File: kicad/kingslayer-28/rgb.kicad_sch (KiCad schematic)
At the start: 36 parts, among them IC2 IS31FL3731-QFLS2-TR

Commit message: assign some footprints
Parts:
- D29, D30, D31, D32, D33, D34, D35, D36, D37, D38, D39, D40, D41, D42, D43, D44, D45, D46, D47, D48, D49, D50, D51, D52, D53, D54, D55, D56: footprint (none) -> acheron_Components:LED_RGB_SMD_6028_2.8x3.5mm
- IC2: footprint QFN40P400X400X80-29N -> IS31FL3731-QFLS2-TR:QFN40P400X400X80-29N
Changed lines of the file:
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@@
       (effects (font (size 1.27 1.27)) (justify left))
     )
-    (property "Footprint" "" (at 76.2 78.74 0)
+    (property "Footprint" "acheron_Components:LED_RGB_SMD_6028_2.8x3.5mm" (at 76.2 78.74 0)
       (effects (font (size 1.27 1.27)) hide)
     )
@@
       (effects (font (size 1.27 1.27)) (justify left))
     )
-    (property "Footprint" "" (at 57.15 111.76 0)
+    (property "Footprint" "acheron_Components:LED_RGB_SMD_6028_2.8x3.5mm" (at 57.15 111.76 0)
       (effects (font (size 1.27 1.27)) hide)
     )
@@
       (effects (font (size 1.27 1.27)) (justify left))
     )
-    (property "Footprint" "" (at 95.25 111.76 0)
+    (property "Footprint" "acheron_Components:LED_RGB_SMD_6028_2.8x3.5mm" (at 95.25 111.76 0)
       (effects (font (size 1.27 1.27)) hide)
     )
@@
     )
     (property "Footprint" "" (at 259.08 133.35 0)
-      (effects (font (size 1.524 1.524)))
+      (effects (font (size 1.524 1.524)) hide)
     )
     (property "Datasheet" "" (at 259.08 133.35 0)
@@
       (effects (font (size 1.27 1.27)) (justify left))
     )
-    (property "Footprint" "" (at 57.15 78.74 0)
+    (property "Footprint" "acheron_Components:LED_RGB_SMD_6028_2.8x3.5mm" (at 57.15 78.74 0)
       (effects (font (size 1.27 1.27)) hide)
     )
@@
       (effects (font (size 1.27 1.27)) (justify left))
     )
-    (property "Footprint" "" (at 38.1 144.78 0)
+    (property "Footprint" "acheron_Components:LED_RGB_SMD_6028_2.8x3.5mm" (at 38.1 144.78 0)
       (effects (font (size 1.27 1.27)) hide)
     )
@@
       (effects (font (size 1.27 1.27)) (justify left))
     )
-    (property "Footprint" "" (at 57.15 45.72 0)
+    (property "Footprint" "acheron_Components:LED_RGB_SMD_6028_2.8x3.5mm" (at 57.15 45.72 0)
       (effects (font (size 1.27 1.27)) hide)
     )
@@
       (effects (font (size 1.27 1.27)) (justify left))
     )
-    (property "Footprint" "" (at 38.1 45.72 0)
+    (property "Footprint" "acheron_Components:LED_RGB_SMD_6028_2.8x3.5mm" (at 38.1 45.72 0)
       (effects (font (size 1.27 1.27)) hide)
     )
@@
       (effects (font (size 1.27 1.27)) (justify left))
     )
-    (property "Footprint" "" (at 99.06 177.8 0)
+    (property "Footprint" "acheron_Components:LED_RGB_SMD_6028_2.8x3.5mm" (at 99.06 177.8 0)
       (effects (font (size 1.27 1.27)) hide)
     )
@@
     )
     (property "Footprint" "" (at 190.5 146.05 0)
-      (effects (font (size 1.524 1.524)))
+      (effects (font (size 1.524 1.524)) hide)
     )
     (property "Datasheet" "~" (at 190.5 146.05 0)
@@
       (effects (font (size 1.27 1.27)) (justify left))
     )
-    (property "Footprint" "" (at 133.35 144.78 0)
+    (property "Footprint" "acheron_Components:LED_RGB_SMD_6028_2.8x3.5mm" (at 133.35 144.78 0)
       (effects (font (size 1.27 1.27)) hide)
     )
@@
       (effects (font (size 1.27 1.27)) (justify left))
     )
-    (property "Footprint" "" (at 57.15 177.8 0)
+    (property "Footprint" "acheron_Components:LED_RGB_SMD_6028_2.8x3.5mm" (at 57.15 177.8 0)
       (effects (font (size 1.27 1.27)) hide)
     )
@@
       (effects (font (size 1.27 1.27)) (justify left))
     )
-    (property "Footprint" "" (at 118.11 177.8 0)
+    (property "Footprint" "acheron_Components:LED_RGB_SMD_6028_2.8x3.5mm" (at 118.11 177.8 0)
       (effects (font (size 1.27 1.27)) hide)
     )
@@
     )
     (property "Footprint" "" (at 198.12 50.8 0)
-      (effects (font (size 1.524 1.524)))
+      (effects (font (size 1.524 1.524)) hide)
     )
     (property "Datasheet" "" (at 198.12 50.8 0)
@@
       (effects (font (size 1.27 1.27)) (justify left))
     )
-    (property "Footprint" "" (at 38.1 111.76 0)
+    (property "Footprint" "acheron_Components:LED_RGB_SMD_6028_2.8x3.5mm" (at 38.1 111.76 0)
       (effects (font (size 1.27 1.27)) hide)
     )
@@
       (effects (font (size 1.27 1.27)) (justify left))
     )
-    (property "Footprint" "" (at 114.3 111.76 0)
+    (property "Footprint" "acheron_Components:LED_RGB_SMD_6028_2.8x3.5mm" (at 114.3 111.76 0)
       (effects (font (size 1.27 1.27)) hide)
     )
@@
       (effects (font (size 1.27 1.27)) (justify left))
     )
-    (property "Footprint" "" (at 99.06 78.74 0)
+    (property "Footprint" "acheron_Components:LED_RGB_SMD_6028_2.8x3.5mm" (at 99.06 78.74 0)
       (effects (font (size 1.27 1.27)) hide)
     )
@@
     )
     (property "Footprint" "" (at 248.92 132.08 0)
-      (effects (font (size 1.524 1.524)))
+      (effects (font (size 1.524 1.524)) hide)
     )
     (property "Datasheet" "~" (at 248.92 132.08 0)
@@
       (effects (font (size 1.27 1.27)) (justify left))
     )
-    (property "Footprint" "" (at 114.3 45.72 0)
+    (property "Footprint" "acheron_Components:LED_RGB_SMD_6028_2.8x3.5mm" (at 114.3 45.72 0)
       (effects (font (size 1.27 1.27)) hide)
     )
@@
       (effects (font (size 1.27 1.27)) (justify left))
     )
-    (property "Footprint" "" (at 133.35 45.72 0)
+    (property "Footprint" "acheron_Components:LED_RGB_SMD_6028_2.8x3.5mm" (at 133.35 45.72 0)
       (effects (font (size 1.27 1.27)) hide)
     )
@@
     )
     (property "Footprint" "" (at 208.28 125.73 0)
-      (effects (font (size 1.524 1.524)))
+      (effects (font (size 1.524 1.524)) hide)
     )
     (property "Datasheet" "~" (at 208.28 125.73 0)
@@
       (effects (font (size 1.27 1.27)) (justify left))
     )
-    (property "Footprint" "" (at 76.2 111.76 0)
+    (property "Footprint" "acheron_Components:LED_RGB_SMD_6028_2.8x3.5mm" (at 76.2 111.76 0)
       (effects (font (size 1.27 1.27)) hide)
     )
@@
       (effects (font (size 1.27 1.27)) (justify left))
     )
-    (property "Footprint" "" (at 95.25 144.78 0)
+    (property "Footprint" "acheron_Components:LED_RGB_SMD_6028_2.8x3.5mm" (at 95.25 144.78 0)
       (effects (font (size 1.27 1.27)) hide)
     )
@@
       (effects (font (size 1.27 1.27)) (justify left))
     )
-    (property "Footprint" "" (at 95.25 45.72 0)
+    (property "Footprint" "acheron_Components:LED_RGB_SMD_6028_2.8x3.5mm" (at 95.25 45.72 0)
       (effects (font (size 1.27 1.27)) hide)
     )
@@
       (effects (font (size 1.27 1.27)) (justify left))
     )
-    (property "Footprint" "" (at 76.2 144.78 0)
+    (property "Footprint" "acheron_Components:LED_RGB_SMD_6028_2.8x3.5mm" (at 76.2 144.78 0)
       (effects (font (size 1.27 1.27)) hide)
     )
@@
       (effects (font (size 1.27 1.27)) (justify left))
     )
-    (property "Footprint" "" (at 38.1 177.8 0)
+    (property "Footprint" "acheron_Components:LED_RGB_SMD_6028_2.8x3.5mm" (at 38.1 177.8 0)
       (effects (font (size 1.27 1.27)) hide)
     )
@@
       (effects (font (size 1.27 1.27)) (justify left))
     )
-    (property "Footprint" "" (at 76.2 45.72 0)
+    (property "Footprint" "acheron_Components:LED_RGB_SMD_6028_2.8x3.5mm" (at 76.2 45.72 0)
       (effects (font (size 1.27 1.27)) hide)
     )
@@
     )
     (property "Footprint" "" (at 199.39 125.73 0)
-      (effects (font (size 1.524 1.524)))
+      (effects (font (size 1.524 1.524)) hide)
     )
     (property "Datasheet" "~" (at 199.39 125.73 0)
@@
       (effects (font (size 1.27 1.27)))
     )
-    (property "Footprint" "QFN40P400X400X80-29N" (at 240.03 43.18 0)
+    (property "Footprint" "IS31FL3731-QFLS2-TR:QFN40P400X400X80-29N" (at 240.03 43.18 0)
       (effects (font (size 1.27 1.27)) (justify left) hide)
     )
@@
       (effects (font (size 1.27 1.27)) (justify left))
     )
-    (property "Footprint" "" (at 158.75 45.72 0)
+    (property "Footprint" "acheron_Components:LED_RGB_SMD_6028_2.8x3.5mm" (at 158.75 45.72 0)
       (effects (font (size 1.27 1.27)) hide)
     )
@@
       (effects (font (size 1.27 1.27)) (justify left))
     )
-    (property "Footprint" "" (at 118.11 78.74 0)
+    (property "Footprint" "acheron_Components:LED_RGB_SMD_6028_2.8x3.5mm" (at 118.11 78.74 0)
       (effects (font (size 1.27 1.27)) hide)
     )
@@
       (effects (font (size 1.27 1.27)) (justify left))
     )
-    (property "Footprint" "" (at 57.15 144.78 0)
+    (property "Footprint" "acheron_Components:LED_RGB_SMD_6028_2.8x3.5mm" (at 57.15 144.78 0)
       (effects (font (size 1.27 1.27)) hide)
     )
@@
     )
     (property "Footprint" "" (at 190.5 125.73 0)
-      (effects (font (size 1.524 1.524)))
+      (effects (font (size 1.524 1.524)) hide)
     )
     (property "Datasheet" "~" (at 190.5 125.73 0)
@@
       (effects (font (size 1.27 1.27)) (justify left))
     )
-    (property "Footprint" "" (at 114.3 144.78 0)
+    (property "Footprint" "acheron_Components:LED_RGB_SMD_6028_2.8x3.5mm" (at 114.3 144.78 0)
       (effects (font (size 1.27 1.27)) hide)
     )
@@
       (effects (font (size 1.27 1.27)) (justify left))
     )
-    (property "Footprint" "" (at 38.1 78.74 0)
+    (property "Footprint" "acheron_Components:LED_RGB_SMD_6028_2.8x3.5mm" (at 38.1 78.74 0)
       (effects (font (size 1.27 1.27)) hide)
     )
@@
       (effects (font (size 1.27 1.27)) (justify left))
     )
-    (property "Footprint" "" (at 76.2 177.8 0)
-      (effects (font (size 1.27 1.27)) hide)
-    )
+    (property "Footprint" "acheron_Components:LED_RGB_SMD_6028_2.8x3.5mm" (at 76.2 177.8 0)
+      (effects (font (size 1.27 1.27)) hide)
+    )

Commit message: footprint mapping
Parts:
- C8: footprint (none) -> 08053C104KAT2A:CAPC2012X94N
- C9: footprint (none) -> Capacitor_SMD:C_0805_2012Metric_Pad1.18x1.45mm_HandSolder
- R2: footprint (none) -> CR0805-JW-203ELF:RESC2012X60N
- R3, R4, R5: footprint (none) -> Resistor_SMD:R_1206_3216Metric_Pad1.30x1.75mm_HandSolder
- R6: footprint (none) -> RMCF0805JT100K:RESC2012X65N
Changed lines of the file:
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@@
       (effects (font (size 1.27 1.27)) (justify left))
     )
-    (property "Footprint" "" (at 259.08 133.35 0)
+    (property "Footprint" "08053C104KAT2A:CAPC2012X94N" (at 259.08 133.35 0)
       (effects (font (size 1.524 1.524)) hide)
     )
@@
       (effects (font (size 1.27 1.27)) (justify left))
     )
-    (property "Footprint" "" (at 190.5 146.05 0)
+    (property "Footprint" "RMCF0805JT100K:RESC2012X65N" (at 190.5 146.05 0)
       (effects (font (size 1.524 1.524)) hide)
     )
@@
       (effects (font (size 1.27 1.27)) (justify right))
     )
-    (property "Footprint" "" (at 198.12 50.8 0)
+    (property "Footprint" "Capacitor_SMD:C_0805_2012Metric_Pad1.18x1.45mm_HandSolder" (at 198.12 50.8 0)
       (effects (font (size 1.524 1.524)) hide)
     )
@@
       (effects (font (size 1.27 1.27)) (justify left))
     )
-    (property "Footprint" "" (at 248.92 132.08 0)
+    (property "Footprint" "CR0805-JW-203ELF:RESC2012X60N" (at 248.92 132.08 0)
       (effects (font (size 1.524 1.524)) hide)
     )
@@
       (effects (font (size 1.27 1.27)) (justify left))
     )
-    (property "Footprint" "" (at 208.28 125.73 0)
+    (property "Footprint" "Resistor_SMD:R_1206_3216Metric_Pad1.30x1.75mm_HandSolder" (at 208.28 125.73 0)
       (effects (font (size 1.524 1.524)) hide)
     )
@@
       (effects (font (size 1.27 1.27)) (justify left))
     )
-    (property "Footprint" "" (at 199.39 125.73 0)
+    (property "Footprint" "Resistor_SMD:R_1206_3216Metric_Pad1.30x1.75mm_HandSolder" (at 199.39 125.73 0)
       (effects (font (size 1.524 1.524)) hide)
     )
@@
       (effects (font (size 1.27 1.27)) (justify left))
     )
-    (property "Footprint" "" (at 190.5 125.73 0)
+    (property "Footprint" "Resistor_SMD:R_1206_3216Metric_Pad1.30x1.75mm_HandSolder" (at 190.5 125.73 0)
       (effects (font (size 1.524 1.524)) hide)
     )

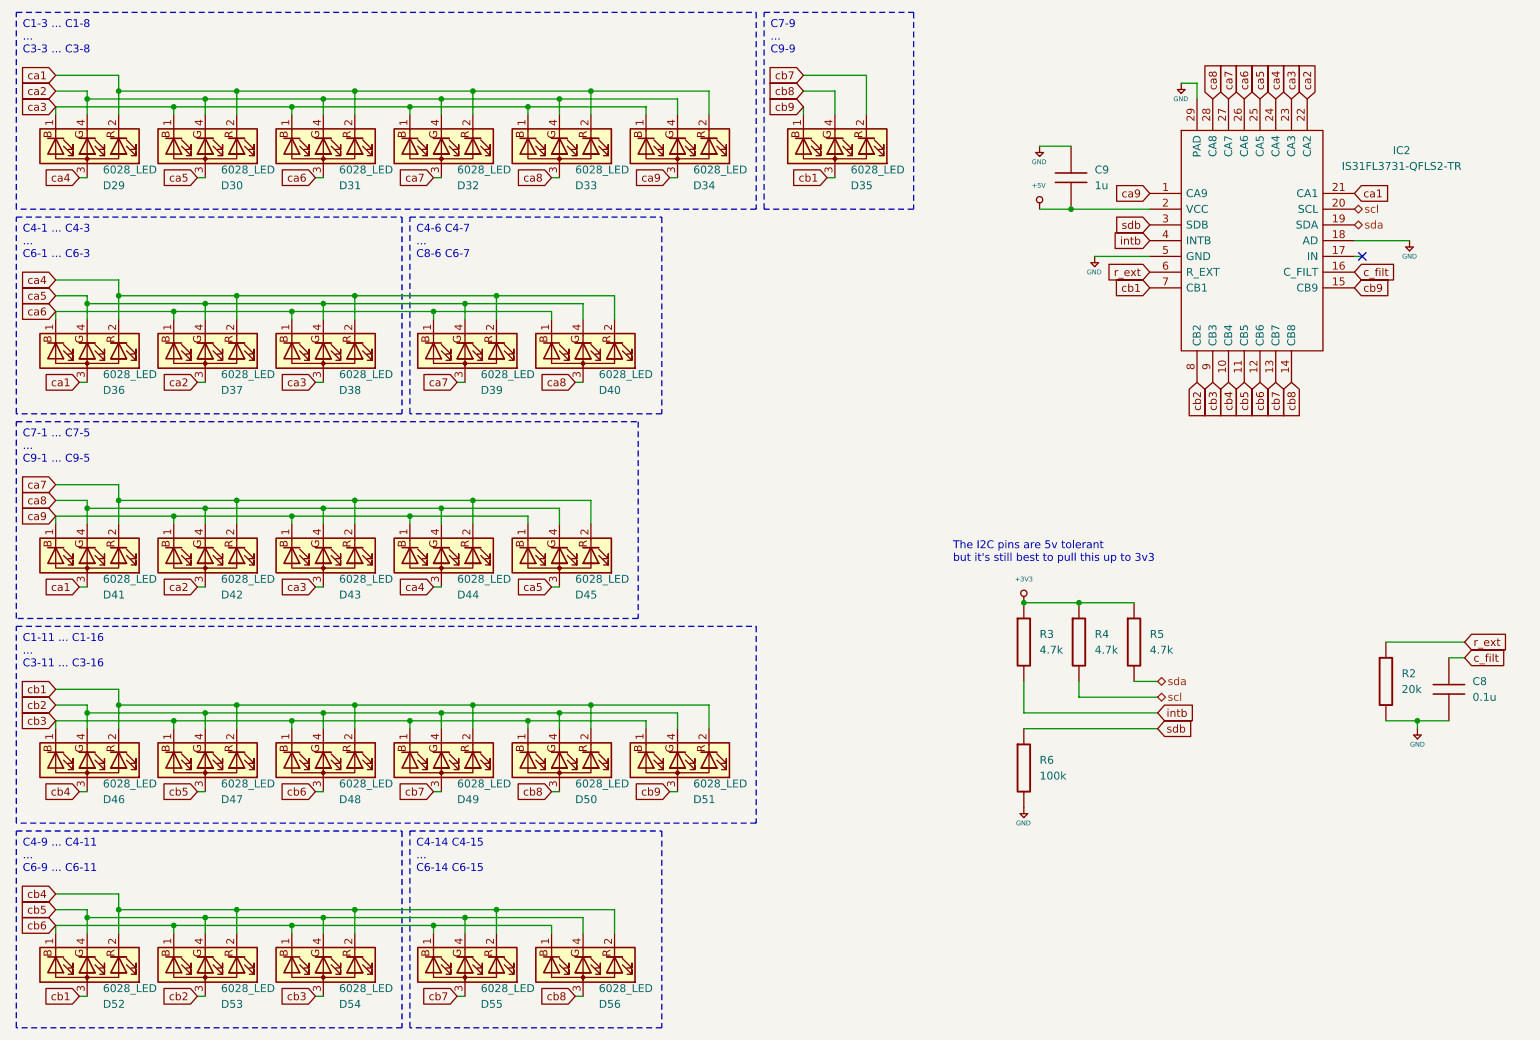
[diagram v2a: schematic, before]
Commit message: finish footprint picking
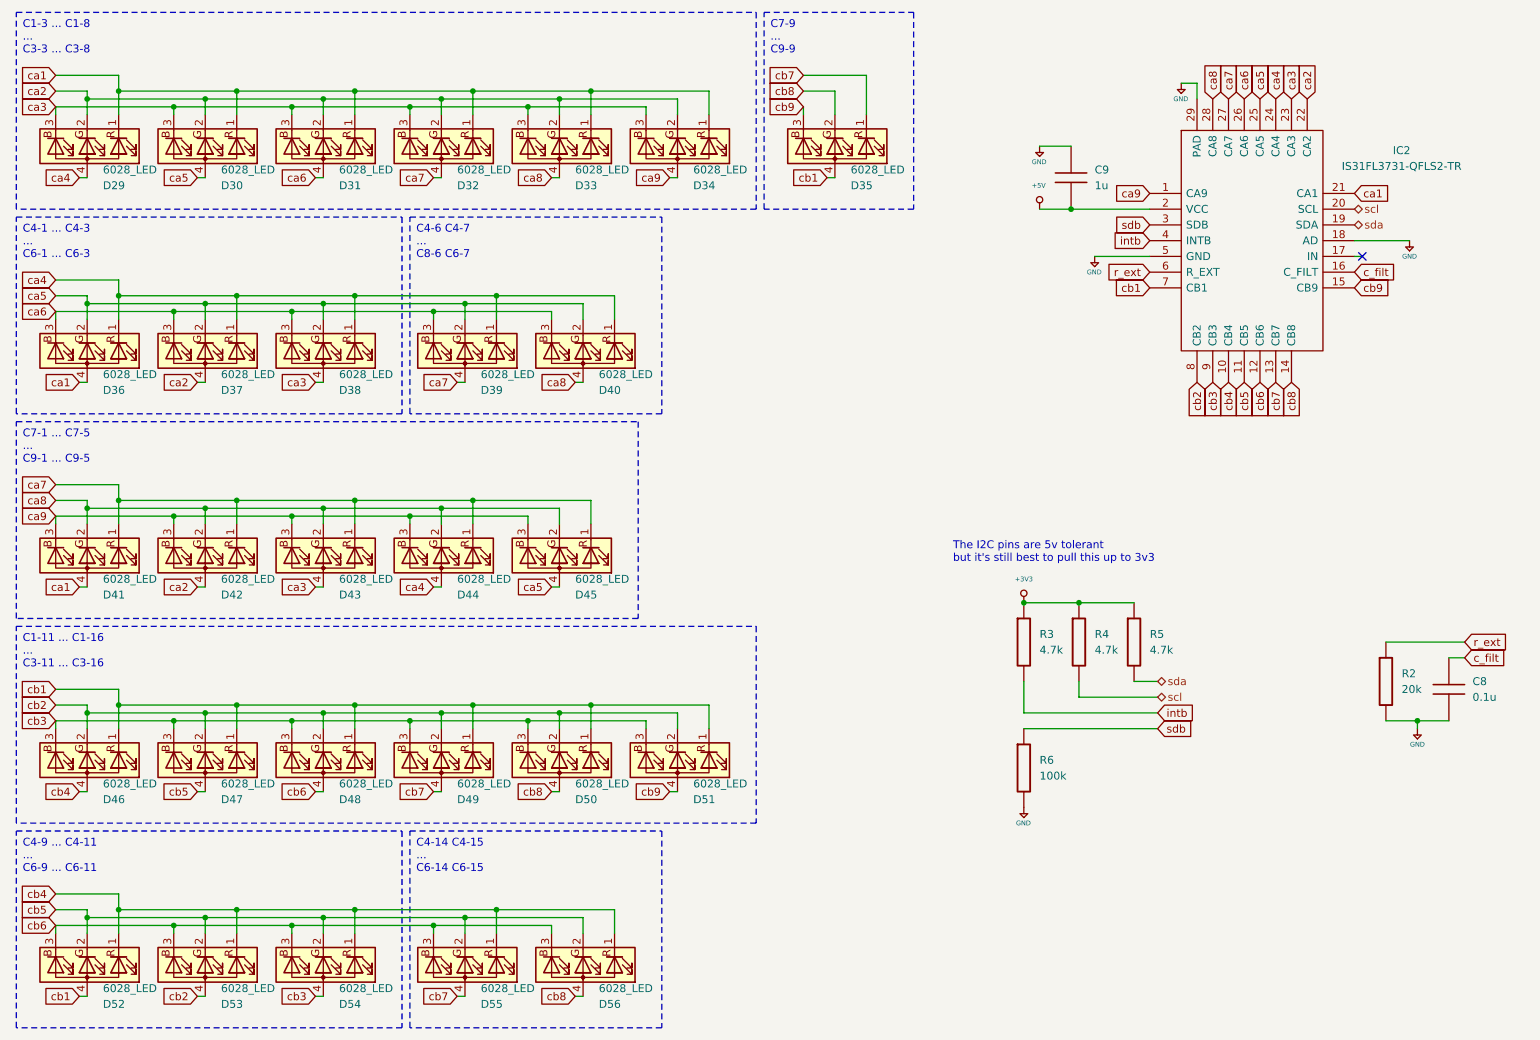
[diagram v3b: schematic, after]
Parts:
- D29, D30, D31, D32, D33, D34, D35, D36, D37, D38, D39, D40, D41, D42, D43, D44, D45, D46, D47, D48, D49, D50, D51, D52, D53, D54, D55, D56: footprint acheron_Components:LED_RGB_SMD_6028_2.8x3.5mm -> LED_SMD:LED_RGB_1210; symbol Device:LED_BRAG -> Device:LED_RGBA
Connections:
- net ca1: now also D29.1 (RK), D30.1 (RK), D31.1 (RK), D32.1 (RK), D33.1 (RK), D34.1 (RK), D36.4 (A), D41.4 (A); no longer D29.2 (RK), D30.2 (RK), D31.2 (RK), D32.2 (RK), D33.2 (RK), D34.2 (RK), D36.3 (A), D41.3 (A)
- net ca2: now also D29.2 (GK), D30.2 (GK), D31.2 (GK), D32.2 (GK), D33.2 (GK), D34.2 (GK), D37.4 (A), D42.4 (A); no longer D29.4 (GK), D30.4 (GK), D31.4 (GK), D32.4 (GK), D33.4 (GK), D34.4 (GK), D37.3 (A), D42.3 (A)
- net ca3: now also D29.3 (BK), D30.3 (BK), D31.3 (BK), D32.3 (BK), D33.3 (BK), D34.3 (BK), D38.4 (A), D43.4 (A); no longer D29.1 (BK), D30.1 (BK), D31.1 (BK), D32.1 (BK), D33.1 (BK), D34.1 (BK), D38.3 (A), D43.3 (A)
- net ca4: now also D29.4 (A), D36.1 (RK), D37.1 (RK), D38.1 (RK), D39.1 (RK), D40.1 (RK), D44.4 (A); no longer D29.3 (A), D36.2 (RK), D37.2 (RK), D38.2 (RK), D39.2 (RK), D40.2 (RK), D44.3 (A)
- net ca5: now also D30.4 (A), D36.2 (GK), D37.2 (GK), D38.2 (GK), D39.2 (GK), D40.2 (GK), D45.4 (A); no longer D30.3 (A), D36.4 (GK), D37.4 (GK), D38.4 (GK), D39.4 (GK), D40.4 (GK), D45.3 (A)
- net ca6: now also D31.4 (A), D36.3 (BK), D37.3 (BK), D38.3 (BK), D39.3 (BK), D40.3 (BK); no longer D31.3 (A), D36.1 (BK), D37.1 (BK), D38.1 (BK), D39.1 (BK), D40.1 (BK)
- net ca7: now also D32.4 (A), D39.4 (A), D41.1 (RK), D42.1 (RK), D43.1 (RK), D44.1 (RK), D45.1 (RK); no longer D32.3 (A), D39.3 (A), D41.2 (RK), D42.2 (RK), D43.2 (RK), D44.2 (RK), D45.2 (RK)
- net ca8: now also D33.4 (A), D40.4 (A), D41.2 (GK), D42.2 (GK), D43.2 (GK), D44.2 (GK), D45.2 (GK); no longer D33.3 (A), D40.3 (A), D41.4 (GK), D42.4 (GK), D43.4 (GK), D44.4 (GK), D45.4 (GK)
- net ca9: now also D34.4 (A), D41.3 (BK), D42.3 (BK), D43.3 (BK), D44.3 (BK), D45.3 (BK); no longer D34.3 (A), D41.1 (BK), D42.1 (BK), D43.1 (BK), D44.1 (BK), D45.1 (BK)
- net cb1: now also D35.4 (A), D46.1 (RK), D47.1 (RK), D48.1 (RK), D49.1 (RK), D50.1 (RK), D51.1 (RK), D52.4 (A); no longer D35.3 (A), D46.2 (RK), D47.2 (RK), D48.2 (RK), D49.2 (RK), D50.2 (RK), D51.2 (RK), D52.3 (A)
- net cb2: now also D46.2 (GK), D47.2 (GK), D48.2 (GK), D49.2 (GK), D50.2 (GK), D51.2 (GK), D53.4 (A); no longer D46.4 (GK), D47.4 (GK), D48.4 (GK), D49.4 (GK), D50.4 (GK), D51.4 (GK), D53.3 (A)
- net cb3: now also D46.3 (BK), D47.3 (BK), D48.3 (BK), D49.3 (BK), D50.3 (BK), D51.3 (BK), D54.4 (A); no longer D46.1 (BK), D47.1 (BK), D48.1 (BK), D49.1 (BK), D50.1 (BK), D51.1 (BK), D54.3 (A)
- net cb4: now also D46.4 (A), D52.1 (RK), D53.1 (RK), D54.1 (RK), D55.1 (RK), D56.1 (RK); no longer D46.3 (A), D52.2 (RK), D53.2 (RK), D54.2 (RK), D55.2 (RK), D56.2 (RK)
- net cb5: now also D47.4 (A), D52.2 (GK), D53.2 (GK), D54.2 (GK), D55.2 (GK), D56.2 (GK); no longer D47.3 (A), D52.4 (GK), D53.4 (GK), D54.4 (GK), D55.4 (GK), D56.4 (GK)
- net cb6: now also D48.4 (A), D52.3 (BK), D53.3 (BK), D54.3 (BK), D55.3 (BK), D56.3 (BK); no longer D48.3 (A), D52.1 (BK), D53.1 (BK), D54.1 (BK), D55.1 (BK), D56.1 (BK)
- net cb7: now also D35.1 (RK), D49.4 (A), D55.4 (A); no longer D35.2 (RK), D49.3 (A), D55.3 (A)
- net cb8: now also D35.2 (GK), D50.4 (A), D56.4 (A); no longer D35.4 (GK), D50.3 (A), D56.3 (A)
- net cb9: now also D35.3 (BK), D51.4 (A); no longer D35.1 (BK), D51.3 (A)
